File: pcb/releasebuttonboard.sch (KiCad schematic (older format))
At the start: 5 parts

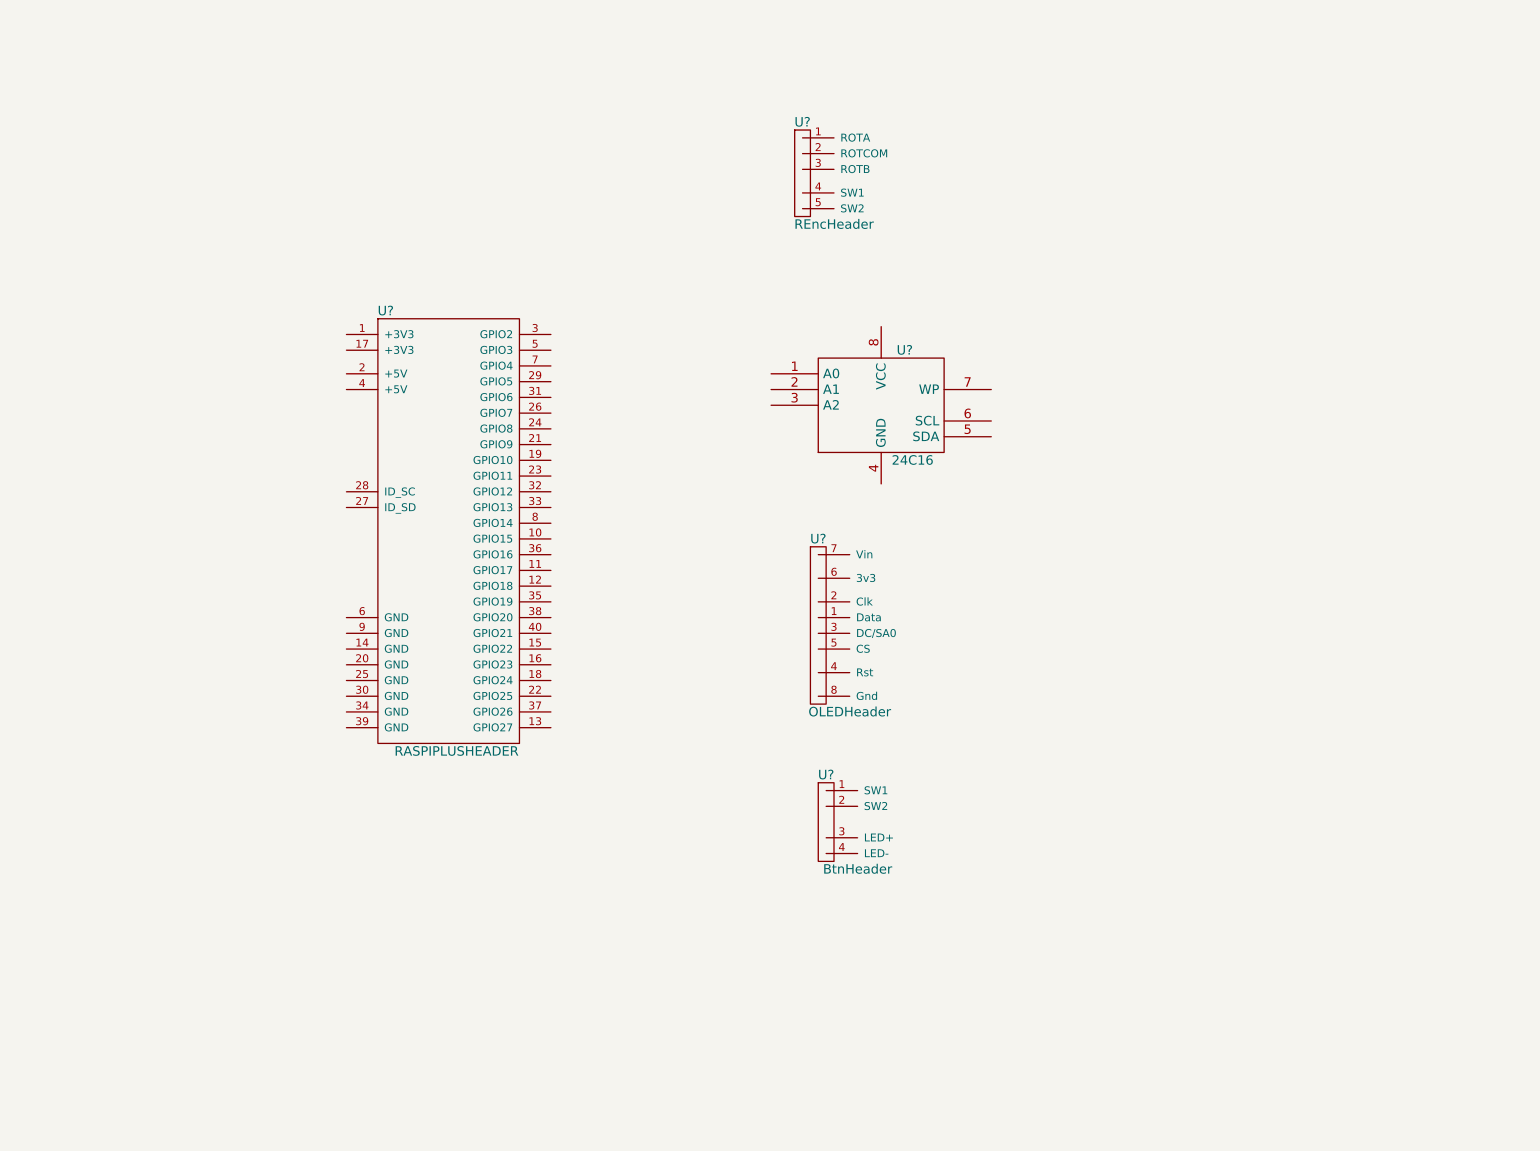
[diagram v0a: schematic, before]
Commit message: Schematic of ID EEPROM subcircuit.
(And some extra bits that crept in.)
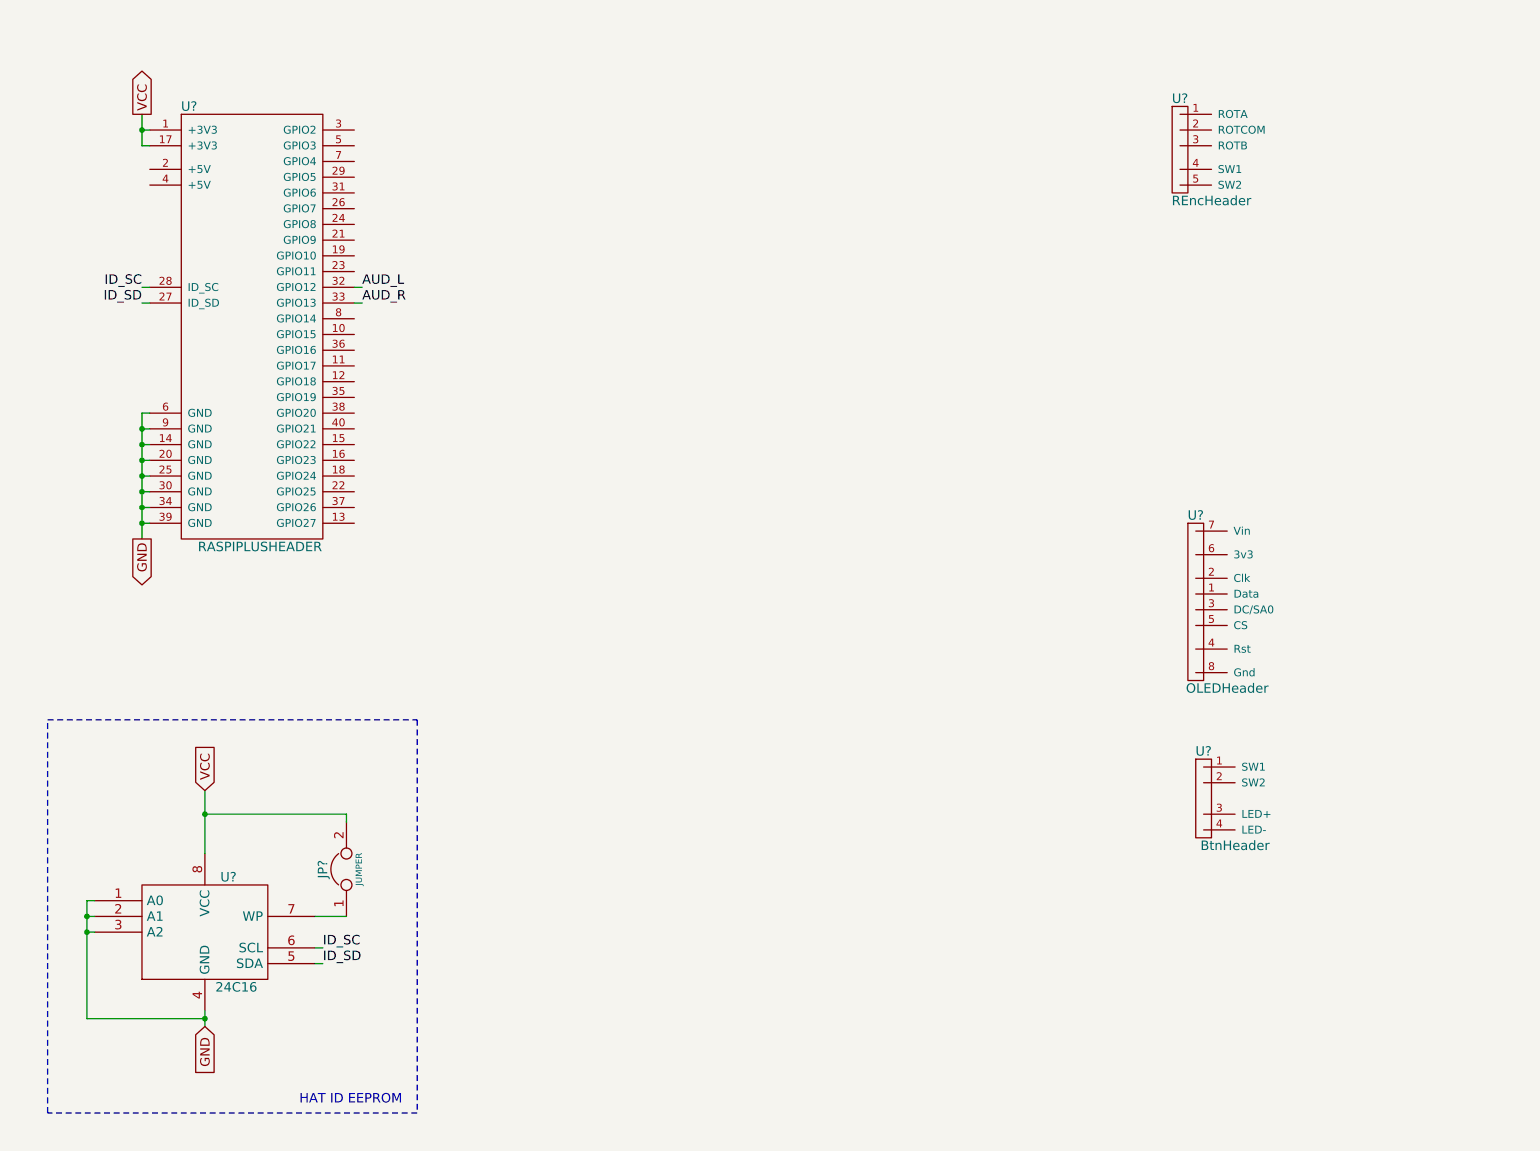
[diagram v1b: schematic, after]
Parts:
- removed U?: 24C16, symbol 24C16
- added JP?: JUMPER, symbol JUMPER
- added U?: 24C16, symbol 24C16
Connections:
- net VCC: now reaches U?.1 (+3V3)
- net VCC: now also U?.17 (+3V3), JP?.2, U?.8 (VCC)
- net GND: now reaches U?.14 (GND)
- net GND: now also U?.20 (GND), U?.25 (GND), U?.30 (GND), U?.34 (GND), U?.39 (GND), U?.6 (GND), U?.9 (GND), U?.1 (A0), U?.2 (A1), U?.3 (A2), U?.4 (GND)
- net ID_SD: now reaches U?.27 (ID_SD)
- net ID_SD: now also U?.5 (SDA)
- net ID_SC: now reaches U?.28 (ID_SC)
- net ID_SC: now also U?.6 (SCL)
- net AUD_L: now reaches U?.32 (GPIO12)
- net AUD_R: now reaches U?.33 (GPIO13)
- new net: JP?.1, U?.7 (WP)
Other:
- note added: "HAT ID EEPROM"
- moved on the sheet: U?
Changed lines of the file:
@@
 LIBS:valves
 LIBS:releasebutton
-EELAYER 25 0
+LIBS:releasebuttonboard-cache
+EELAYER 24 0
 EELAYER END
 $Descr USLetter 11000 8500
@@
 L RASPIPLUSHEADER U?
 U 1 1 54A79B4A
-P 3450 3900
-F 0 "U?" H 3050 5250 60  0000 C CNN
-F 1 "RASPIPLUSHEADER" H 3500 2450 60  0000 C CNN
-F 2 "" H 3450 3650 60  0000 C CNN
-F 3 "" H 3450 3650 60  0000 C CNN
-	1    3450 3900
-	1    0    0    -1
-$EndComp
-$Comp
-L 24C16 U?
-U 1 1 54A7A84F
-P 6200 3150
-F 0 "U?" H 6350 3500 60  0000 C CNN
-F 1 "24C16" H 6400 2800 60  0000 C CNN
-F 2 "" H 6200 3150 60  0000 C CNN
-F 3 "" H 6200 3150 60  0000 C CNN
-	1    6200 3150
+P 2200 2600
+F 0 "U?" H 1800 3950 60  0000 C CNN
+F 1 "RASPIPLUSHEADER" H 2250 1150 60  0000 C CNN
+F 2 "" H 2200 2350 60  0000 C CNN
+F 3 "" H 2200 2350 60  0000 C CNN
+	1    2200 2600
 	1    0    0    -1
 $EndComp
@@
 L OLEDHeader U?
 U 1 1 54A7A9C0
-P 5800 4500
-F 0 "U?" H 5800 5000 60  0000 C CNN
-F 1 "OLEDHeader" H 6000 3900 60  0000 C CNN
-F 2 "" H 5800 4700 60  0000 C CNN
-F 3 "" H 5800 4700 60  0000 C CNN
-	1    5800 4500
+P 8200 4350
+F 0 "U?" H 8200 4850 60  0000 C CNN
+F 1 "OLEDHeader" H 8400 3750 60  0000 C CNN
+F 2 "" H 8200 4550 60  0000 C CNN
+F 3 "" H 8200 4550 60  0000 C CNN
+	1    8200 4350
 	1    0    0    -1
 $EndComp
@@
 L BtnHeader U?
 U 1 1 54A7AA14
-P 5850 5800
-F 0 "U?" H 5850 6100 60  0000 C CNN
-F 1 "BtnHeader" H 6050 5500 60  0000 C CNN
-F 2 "" H 5850 5850 60  0000 C CNN
-F 3 "" H 5850 5850 60  0000 C CNN
-	1    5850 5800
+P 8250 5650
+F 0 "U?" H 8250 5950 60  0000 C CNN
+F 1 "BtnHeader" H 8450 5350 60  0000 C CNN
+F 2 "" H 8250 5700 60  0000 C CNN
+F 3 "" H 8250 5700 60  0000 C CNN
+	1    8250 5650
 	1    0    0    -1
 $EndComp
@@
 L REncHeader U?
 U 1 1 54A7ABB1
-P 5700 1700
-F 0 "U?" H 5700 2050 60  0000 C CNN
-F 1 "REncHeader" H 5900 1400 60  0000 C CNN
-F 2 "" H 5700 1750 60  0000 C CNN
-F 3 "" H 5700 1750 60  0000 C CNN
-	1    5700 1700
+P 8100 1550
+F 0 "U?" H 8100 1900 60  0000 C CNN
+F 1 "REncHeader" H 8300 1250 60  0000 C CNN
+F 2 "" H 8100 1600 60  0000 C CNN
+F 3 "" H 8100 1600 60  0000 C CNN
+	1    8100 1550
 	1    0    0    -1
 $EndComp
+$Comp
+L 24C16 U?
+U 1 1 54A83FFB
+P 1900 6500
+F 0 "U?" H 2050 6850 60  0000 C CNN
+F 1 "24C16" H 2100 6150 60  0000 C CNN
+F 2 "" H 1900 6500 60  0000 C CNN
+F 3 "" H 1900 6500 60  0000 C CNN
+	1    1900 6500
+	1    0    0    -1
+$EndComp
+Text GLabel 1500 4000 3    60   Output ~ 0
+GND
+Wire Wire Line
+	1550 3200 1500 3200
+Wire Wire Line
+	1500 3200 1500 4000
+Wire Wire Line
+	1550 3300 1500 3300
+Connection ~ 1500 3300
+Wire Wire Line
+	1550 3400 1500 3400
+Connection ~ 1500 3400
+Wire Wire Line
+	1550 3500 1500 3500
+Connection ~ 1500 3500
+Wire Wire Line
+	1550 3600 1500 3600
+Connection ~ 1500 3600
+Wire Wire Line
+	1550 3700 1500 3700
+Connection ~ 1500 3700
+Wire Wire Line
+	1550 3800 1500 3800
+Connection ~ 1500 3800
+Wire Wire Line
+	1550 3900 1500 3900
+Connection ~ 1500 3900
+Text GLabel 1500 1300 1    60   Output ~ 0
+VCC
+Wire Wire Line
+	1500 1300 1500 1500
+Wire Wire Line
+	1500 1500 1550 1500
+Wire Wire Line
+	1550 1400 1500 1400
+Connection ~ 1500 1400
+Text Label 1500 2400 2    60   ~ 0
+ID_SC
+Text Label 1500 2500 2    60   ~ 0
+ID_SD
+Wire Wire Line
+	1500 2400 1550 2400
+Wire Wire Line
+	1500 2500 1550 2500
+Text GLabel 1900 5600 1    60   Input ~ 0
+VCC
+Text GLabel 1900 7100 3    60   Input ~ 0
+GND
+Wire Wire Line
+	1900 5600 1900 6000
+Wire Wire Line
+	1900 7000 1900 7100
+Wire Wire Line
+	1900 7050 1150 7050
+Wire Wire Line
+	1150 7050 1150 6300
+Wire Wire Line
+	1150 6300 1200 6300
+Connection ~ 1900 7050
+Wire Wire Line
+	1200 6400 1150 6400
+Connection ~ 1150 6400
+Wire Wire Line
+	1200 6500 1150 6500
+Connection ~ 1150 6500
+$Comp
+L JUMPER JP?
+U 1 1 54A841ED
+P 2800 6100
+F 0 "JP?" H 2800 6250 60  0000 C CNN
+F 1 "JUMPER" H 2800 6020 40  0000 C CNN
+F 2 "" H 2800 6100 60  0000 C CNN
+F 3 "" H 2800 6100 60  0000 C CNN
+	1    2800 6100
+	0    -1   -1   0
+$EndComp
+Wire Wire Line
+	2800 5800 2800 5750
+Wire Wire Line
+	2800 5750 1900 5750
+Connection ~ 1900 5750
+Wire Wire Line
+	2600 6400 2800 6400
+Text Label 2650 6600 0    60   ~ 0
+ID_SC
+Text Label 2650 6700 0    60   ~ 0
+ID_SD
+Wire Wire Line
+	2600 6600 2650 6600
+Wire Wire Line
+	2600 6700 2650 6700
+Wire Notes Line
+	900  7650 900  5150
+Wire Notes Line
+	900  5150 3250 5150
+Wire Notes Line
+	3250 5150 3250 7650
+Wire Notes Line
+	3250 7650 900  7650
+Text Notes 2500 7600 0    60   ~ 0
+HAT ID EEPROM
+Text Label 2900 2400 0    60   ~ 0
+AUD_L
+Text Label 2900 2500 0    60   ~ 0
+AUD_R
+Wire Wire Line
+	2850 2400 2900 2400
+Wire Wire Line
+	2850 2500 2900 2500
 $EndSCHEMATC

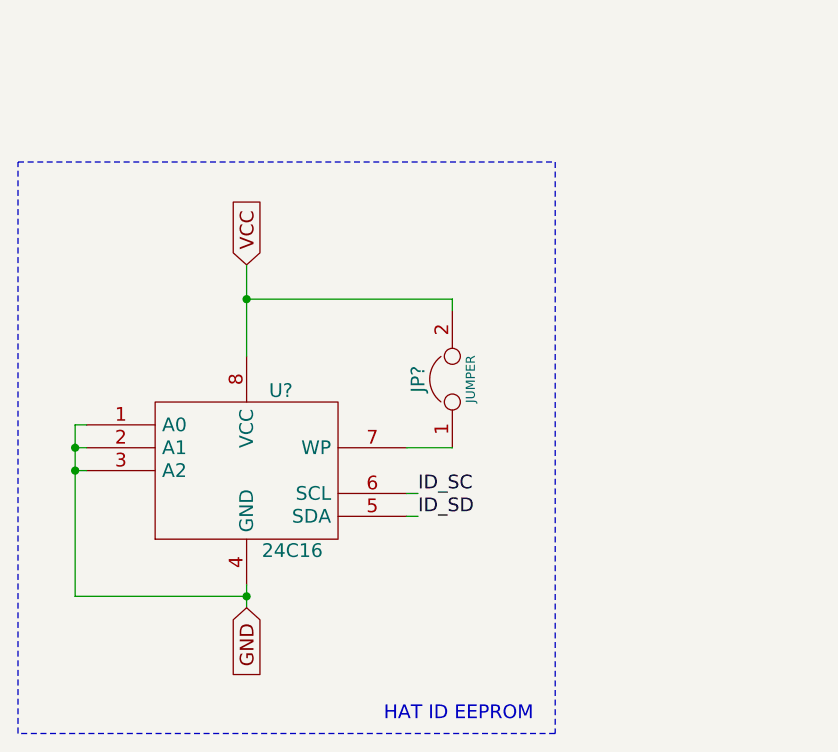
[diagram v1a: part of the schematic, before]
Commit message: Finish the ID EEPROM circuit.
Previously we were missing the necessary IO pin pullups and a decoupling
capacitor.
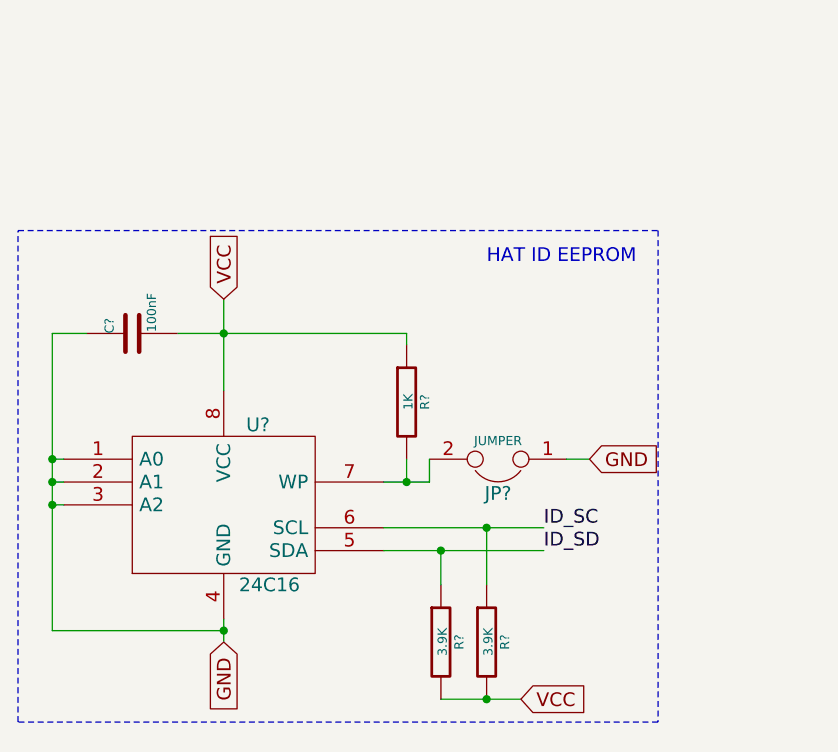
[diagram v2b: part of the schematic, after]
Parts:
- added C?: 100nF, symbol C
- added R?: 1K, symbol R
- added R? (x2): 3.9K, symbol R
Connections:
- net GND: now also JP?.1, C?.1
- net ID_SC: now also R?.1
- net ID_SD: now also R?.1
- net VCC: now also C?.2, R?.1, R?.2, R?.2; no longer JP?.2
- net at U?.7 (WP): now also JP?.2, R?.2; no longer JP?.1
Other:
- moved on the sheet: JP?, U?
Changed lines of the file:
@@
 L 24C16 U?
 U 1 1 54A83FFB
-P 1900 6500
-F 0 "U?" H 2050 6850 60  0000 C CNN
-F 1 "24C16" H 2100 6150 60  0000 C CNN
-F 2 "" H 1900 6500 60  0000 C CNN
-F 3 "" H 1900 6500 60  0000 C CNN
-	1    1900 6500
+P 1800 6650
+F 0 "U?" H 1950 7000 60  0000 C CNN
+F 1 "24C16" H 2000 6300 60  0000 C CNN
+F 2 "" H 1800 6650 60  0000 C CNN
+F 3 "" H 1800 6650 60  0000 C CNN
+	1    1800 6650
 	1    0    0    -1
 $EndComp
@@
 Wire Wire Line
 	1500 2500 1550 2500
-Text GLabel 1900 5600 1    60   Input ~ 0
+Text GLabel 1800 5750 1    60   Input ~ 0
 VCC
-Text GLabel 1900 7100 3    60   Input ~ 0
+Text GLabel 1800 7250 3    60   Input ~ 0
 GND
 Wire Wire Line
-	1900 5600 1900 6000
+	1800 5750 1800 6150
 Wire Wire Line
-	1900 7000 1900 7100
+	1800 7150 1800 7250
 Wire Wire Line
-	1900 7050 1150 7050
+	1050 7200 1800 7200
 Wire Wire Line
-	1150 7050 1150 6300
+	1050 5900 1050 7200
 Wire Wire Line
-	1150 6300 1200 6300
-Connection ~ 1900 7050
+	1050 6450 1100 6450
+Connection ~ 1800 7200
 Wire Wire Line
-	1200 6400 1150 6400
-Connection ~ 1150 6400
+	1100 6550 1050 6550
+Connection ~ 1050 6550
 Wire Wire Line
-	1200 6500 1150 6500
-Connection ~ 1150 6500
+	1100 6650 1050 6650
+Connection ~ 1050 6650
 $Comp
 L JUMPER JP?
 U 1 1 54A841ED
-P 2800 6100
-F 0 "JP?" H 2800 6250 60  0000 C CNN
-F 1 "JUMPER" H 2800 6020 40  0000 C CNN
-F 2 "" H 2800 6100 60  0000 C CNN
-F 3 "" H 2800 6100 60  0000 C CNN
-	1    2800 6100
-	0    -1   -1   0
+P 3000 6450
+F 0 "JP?" H 3000 6600 60  0000 C CNN
+F 1 "JUMPER" H 3000 6370 40  0000 C CNN
+F 2 "" H 3000 6450 60  0000 C CNN
+F 3 "" H 3000 6450 60  0000 C CNN
+	1    3000 6450
+	-1   0    0    1
 $EndComp
-Wire Wire Line
-	2800 5800 2800 5750
-Wire Wire Line
-	2800 5750 1900 5750
-Connection ~ 1900 5750
-Wire Wire Line
-	2600 6400 2800 6400
-Text Label 2650 6600 0    60   ~ 0
+Text Label 3200 6750 0    60   ~ 0
 ID_SC
-Text Label 2650 6700 0    60   ~ 0
+Text Label 3200 6850 0    60   ~ 0
 ID_SD
 Wire Wire Line
-	2600 6600 2650 6600
+	2500 6750 3200 6750
 Wire Wire Line
-	2600 6700 2650 6700
-Wire Notes Line
-	900  7650 900  5150
-Wire Notes Line
-	900  5150 3250 5150
-Wire Notes Line
-	3250 5150 3250 7650
-Wire Notes Line
-	3250 7650 900  7650
-Text Notes 2500 7600 0    60   ~ 0
+	2500 6850 3200 6850
+Text Notes 2950 5600 0    60   ~ 0
 HAT ID EEPROM
 Text Label 2900 2400 0    60   ~ 0
@@
 Wire Wire Line
 	2850 2500 2900 2500
+$Comp
+L C C?
+U 1 1 54A8751D
+P 1400 5900
+F 0 "C?" H 1400 6000 40  0000 L CNN
+F 1 "100nF" H 1406 5815 40  0000 L CNN
+F 2 "" H 1438 5750 30  0000 C CNN
+F 3 "" H 1400 5900 60  0000 C CNN
+	1    1400 5900
+	0    -1   -1   0
+$EndComp
+Wire Wire Line
+	1200 5900 1050 5900
+Connection ~ 1050 6450
+Wire Wire Line
+	1600 5900 2600 5900
+Connection ~ 1800 5900
+$Comp
+L R R?
+U 1 1 54A87661
+P 2600 6200
+F 0 "R?" V 2680 6200 40  0000 C CNN
+F 1 "1K" V 2607 6201 40  0000 C CNN
+F 2 "" V 2530 6200 30  0000 C CNN
+F 3 "" H 2600 6200 30  0000 C CNN
+	1    2600 6200
+	1    0    0    -1
+$EndComp
+Wire Wire Line
+	2600 6550 2600 6450
+Wire Wire Line
+	2600 5900 2600 5950
+Text GLabel 3400 6450 2    60   Input ~ 0
+GND
+$Comp
+L R R?
+U 1 1 54A878B0
+P 2750 7250
+F 0 "R?" V 2830 7250 40  0000 C CNN
+F 1 "3.9K" V 2757 7251 40  0000 C CNN
+F 2 "" V 2680 7250 30  0000 C CNN
+F 3 "" H 2750 7250 30  0000 C CNN
+	1    2750 7250
+	1    0    0    -1
+$EndComp
+$Comp
+L R R?
+U 1 1 54A878C4
+P 2950 7250
+F 0 "R?" V 3030 7250 40  0000 C CNN
+F 1 "3.9K" V 2957 7251 40  0000 C CNN
+F 2 "" V 2880 7250 30  0000 C CNN
+F 3 "" H 2950 7250 30  0000 C CNN
+	1    2950 7250
+	1    0    0    -1
+$EndComp
+Wire Wire Line
+	2500 6550 2700 6550
+Wire Wire Line
+	2700 6550 2700 6450
+Connection ~ 2600 6550
+Wire Wire Line
+	3300 6450 3400 6450
+Wire Wire Line
+	2950 6750 2950 7000
+Connection ~ 2950 6750
+Wire Wire Line
+	2750 6850 2750 7000
+Connection ~ 2750 6850
+Text GLabel 3100 7500 2    60   Input ~ 0
+VCC
+Wire Wire Line
+	2750 7500 3100 7500
+Connection ~ 2950 7500
+Wire Notes Line
+	900  5450 3700 5450
+Wire Notes Line
+	3700 5450 3700 7600
+Wire Notes Line
+	3700 7600 900  7600
+Wire Notes Line
+	900  7600 900  5450
 $EndSCHEMATC
